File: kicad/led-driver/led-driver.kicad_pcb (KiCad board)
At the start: 2 copper layers, 100.3 x 46.4 mm, 44 parts, among them J1 RJ45, J10 Conn_02x06_Odd_Even, J11 Conn_02x06_Odd_Even, J2 RJ45, J3 Conn_01x02_Pin, J4 Conn_02x06_Odd_Even, J5 Conn_02x06_Odd_Even, J6 Conn_02x06_Odd_Even, J7 Conn_02x06_Odd_Even, J8 Conn_02x06_Odd_Even, J9 Conn_02x06_Odd_Even, U1 LP2985-33DBVR, U2 SN65LVDS049, U3 TLC5971PWP

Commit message: Progress
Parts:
- renumbered D12 to D1, D3 to D10, D2 to D11, D1 to D12, D11 to D2, D10 to D3, D9 to D4, D8 to D5, D7 to D6, D6 to D7, D5 to D8, D4 to D9

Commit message: Improve thermal props
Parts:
- moved +V 13.0 mm to (147.8, 86.1)
- moved +3V3 13.0 mm to (144.5, 86.1)
- moved GND 12.9 mm to (151.1, 86.1)
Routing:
- net Net-(D5-K): track 122.6 -> 128.2 mm
- net Net-(D6-K): track 119.6 -> 125.1 mm
- net Net-(D4-K): track 125.5 -> 131.1 mm
- net Net-(D3-K): track 129.2 -> 134.0 mm
- net Net-(D2-K): track 132.6 -> 135.9 mm
- net Net-(D1-K): track 136.2 -> 138.7 mm
- net GND: track 29.6 -> 27.8 mm, vias 14 -> 45
- net Net-(D11-K): track 120.2 -> 119.5 mm
- net Net-(U2-DIN2): track 15.7 -> 15.1 mm
- net Net-(D8-K): track 118.9 -> 119.5 mm
- net Net-(D12-K): track 121.5 -> 121.0 mm

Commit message: Thermal refactoring
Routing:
- net Net-(D8-K): track 119.5 -> 123.9 mm
- net Net-(D7-K): track 119.2 -> 123.6 mm
- net Net-(D10-K): track 119.4 -> 122.8 mm
- net Net-(D9-K): track 119.4 -> 122.4 mm
- net Net-(D6-K): track 125.1 -> 126.9 mm
- net Net-(D11-K): track 119.5 -> 121.0 mm
- net Net-(D3-K): track 134.0 -> 133.4 mm
- net Net-(D4-K): track 131.1 -> 130.5 mm
- net GND: vias 45 -> 54

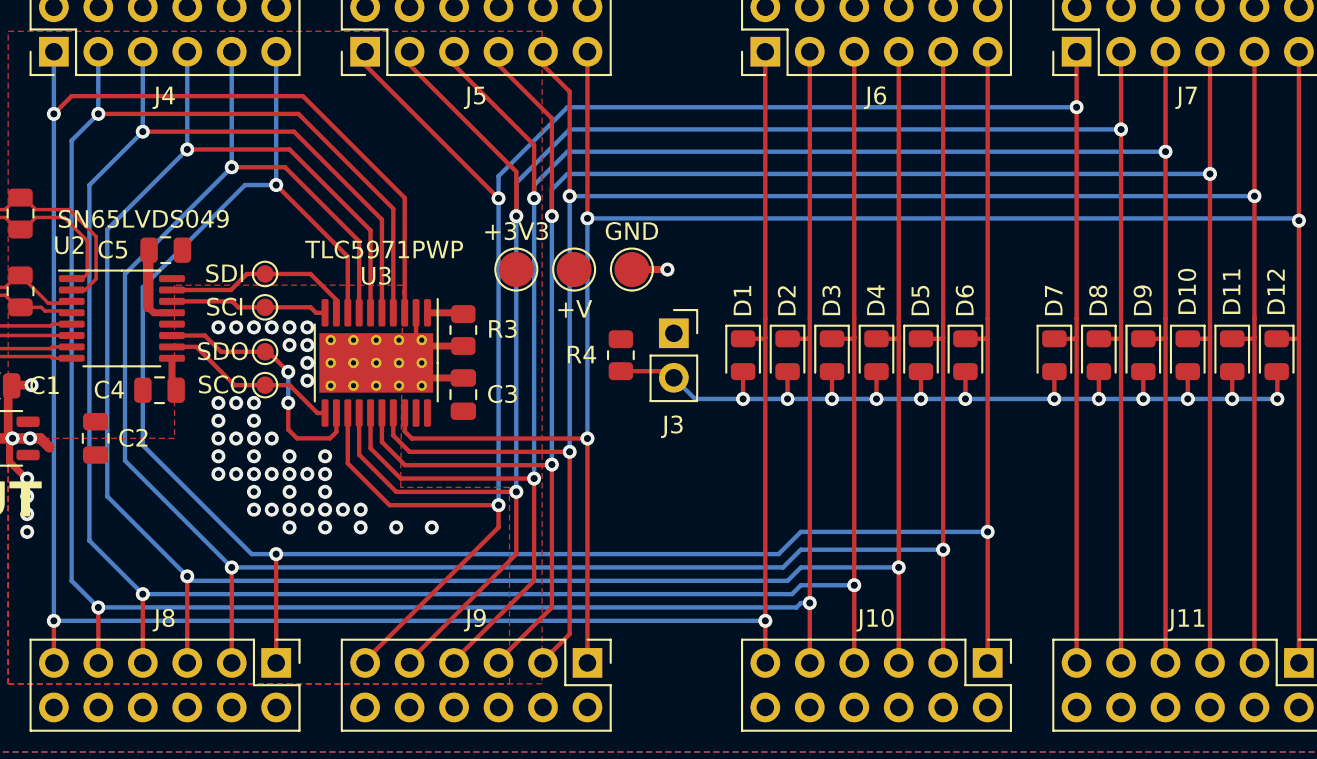
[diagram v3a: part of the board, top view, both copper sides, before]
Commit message: Migrate to 3 chain setup
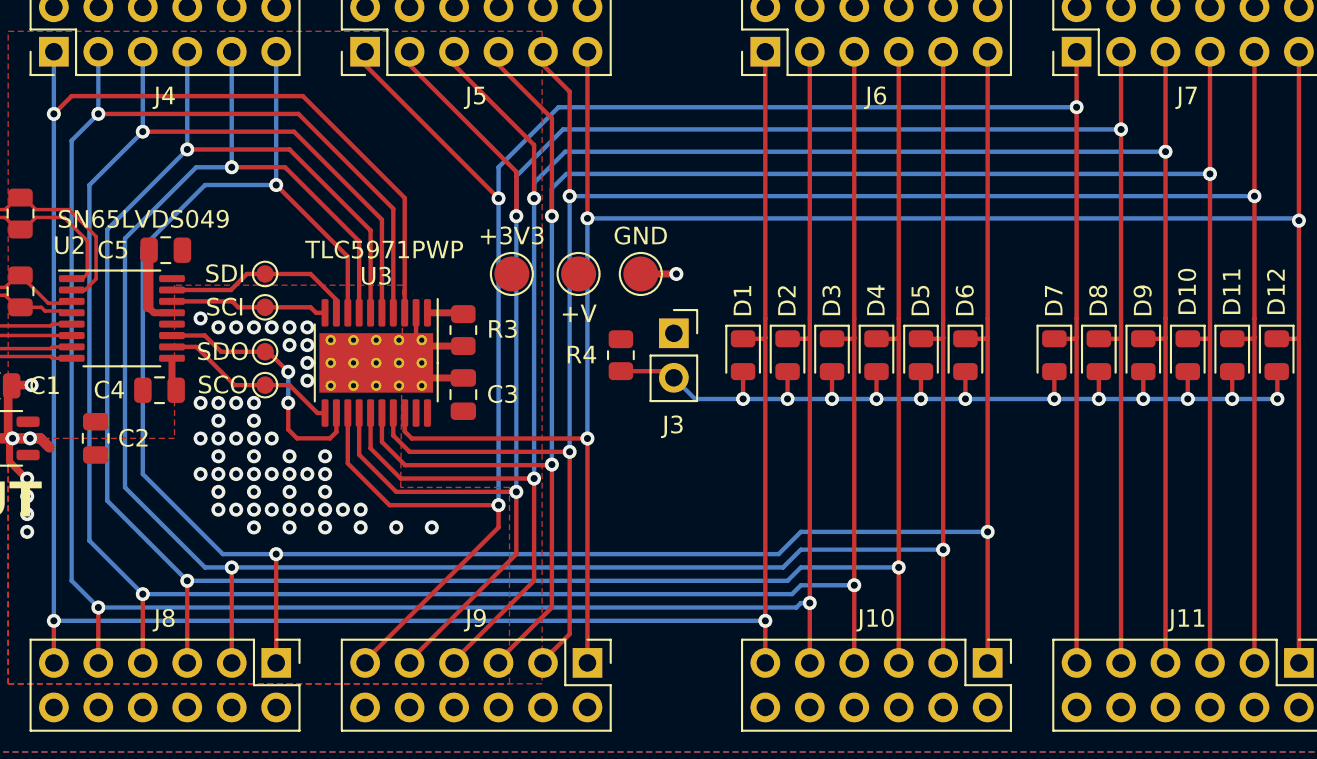
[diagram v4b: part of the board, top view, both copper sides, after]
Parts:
- moved GND 0.57 mm to (151.6, 86.4)
- moved +3V3 0.36 mm to (144.3, 86.4)
- moved +V 0.36 mm to (148.1, 86.4)
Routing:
- net Net-(D6-K): track 126.9 -> 129.2 mm
- net Net-(D5-K): track 127.8 -> 129.9 mm
- net GND: vias 54 -> 62

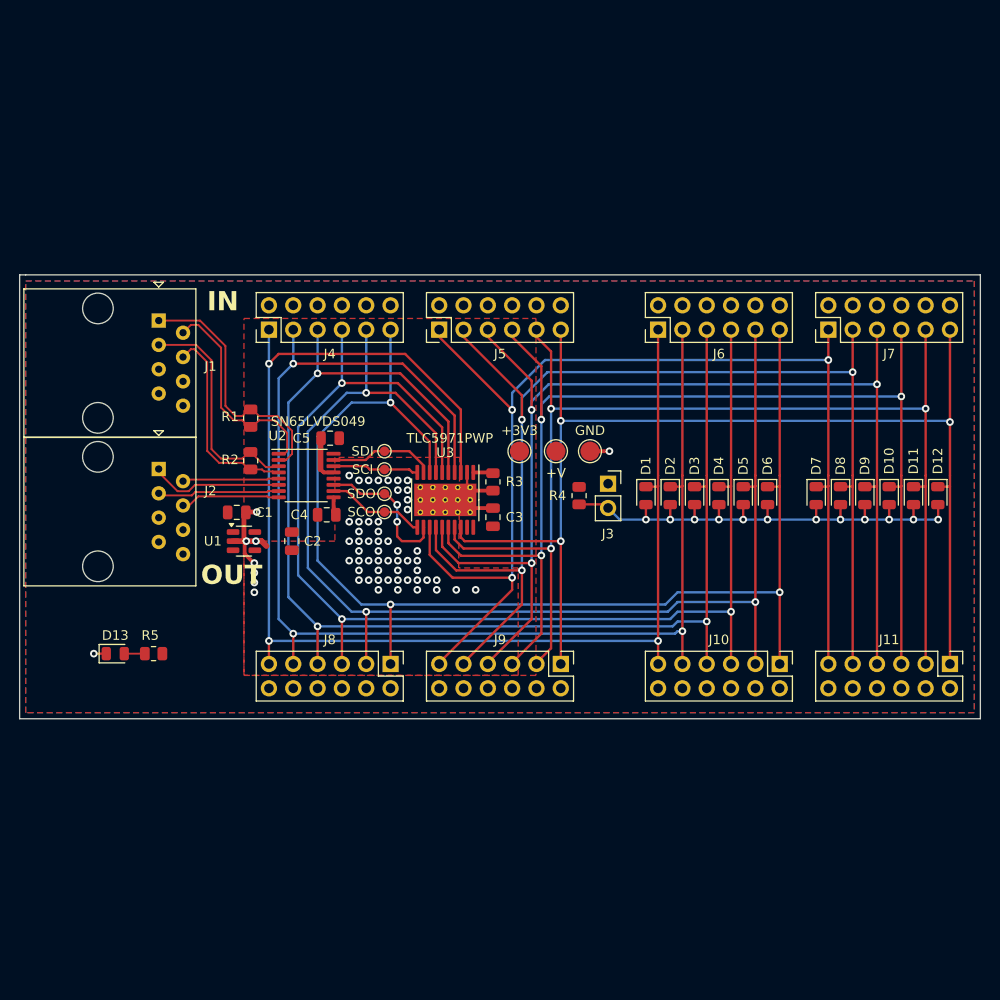
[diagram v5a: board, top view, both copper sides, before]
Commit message: Fix led enumeration
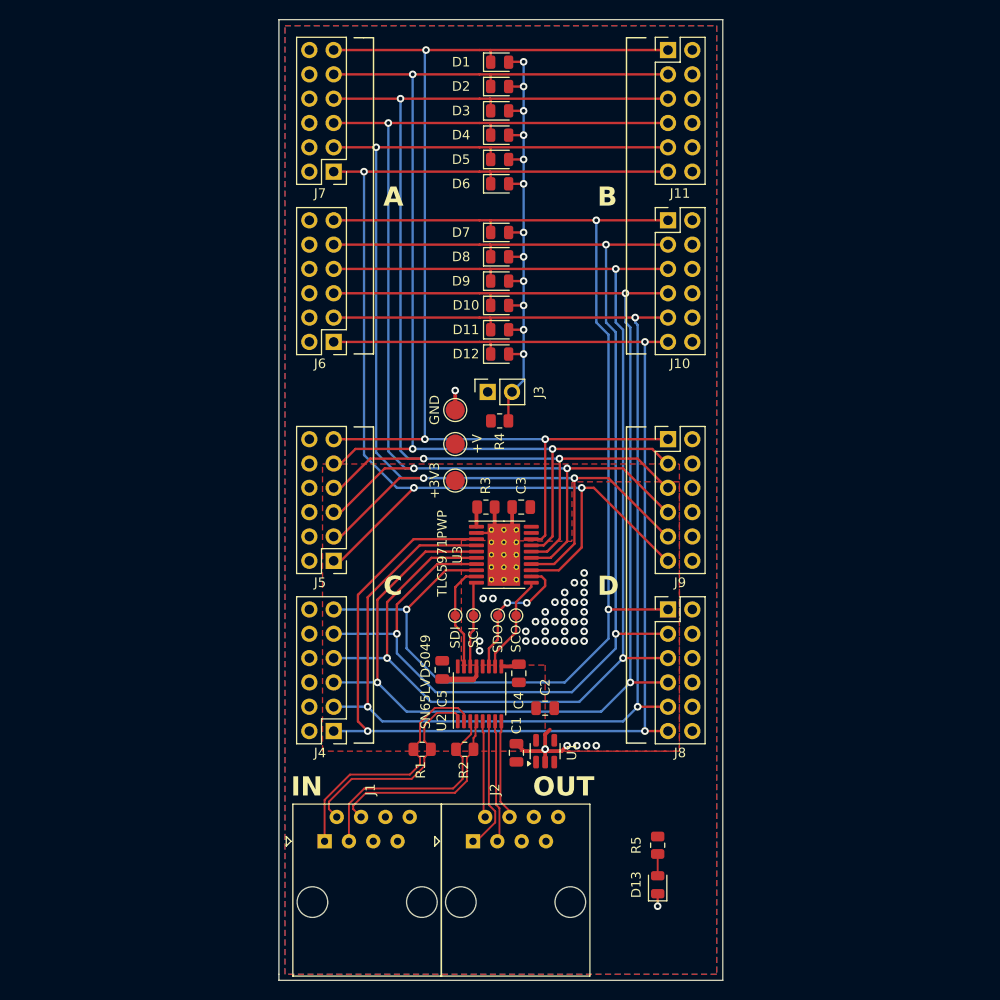
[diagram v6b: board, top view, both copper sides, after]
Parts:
- moved J11 70.6 mm to (159.8, 44.5), turned to 0 degrees
- moved D1 64.4 mm to (142.2, 45.7), turned to 0 degrees
- moved D13 61.6 mm to (158.7, 131.6), turned to 90 degrees
- moved D2 60.8 mm to (142.2, 48.3), turned to 0 degrees
- moved D3 57.2 mm to (142.2, 50.8), turned to 0 degrees
- moved J1 57.1 mm to (123.9, 127.1), turned to 0 degrees
- moved R5 56.3 mm to (158.7, 127.5), turned to -90 degrees
- moved J7 54.2 mm to (124.9, 57.2), turned to 180 degrees
- moved D4 53.6 mm to (142.2, 53.4), turned to 0 degrees
- moved J2 50.9 mm to (139.4, 127.1), turned to 0 degrees
- moved D5 50.0 mm to (142.2, 55.9), turned to 0 degrees
- moved J10 47.8 mm to (159.8, 62.2), turned to 0 degrees
- moved D6 46.4 mm to (142.2, 58.4), turned to 0 degrees
- moved J4 42.5 mm to (124.9, 115.6), turned to 180 degrees
- moved D7 39.2 mm to (142.2, 63.5), turned to 0 degrees
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- renumbered D12 to D1, D3 to D10, D2 to D11, D1 to D12, D11 to D2, D10 to D3, D9 to D4, D8 to D5, D7 to D6, D6 to D7, D5 to D8, D4 to D9
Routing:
- net GND: track 27.8 -> 26.8 mm, vias 62 -> 40
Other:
- board size 100.3 x 46.4 mm -> 46.4 x 100.3 mm
- board text added: "A"
- board text added: "B"
- board text added: "C"
- board text added: "D"

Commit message: Release LEDpcb V0.1 and ESPpcb V0.1
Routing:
- net Net-(D8-K): track 129.9 -> 129.4 mm
